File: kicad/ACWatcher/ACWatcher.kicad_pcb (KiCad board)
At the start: 2 copper layers, 7 parts, among them J1 Intake Temp Sensor, J2 Discharge Temp Sensor, J3 CT Clamp, U1 WeMos_D1_mini

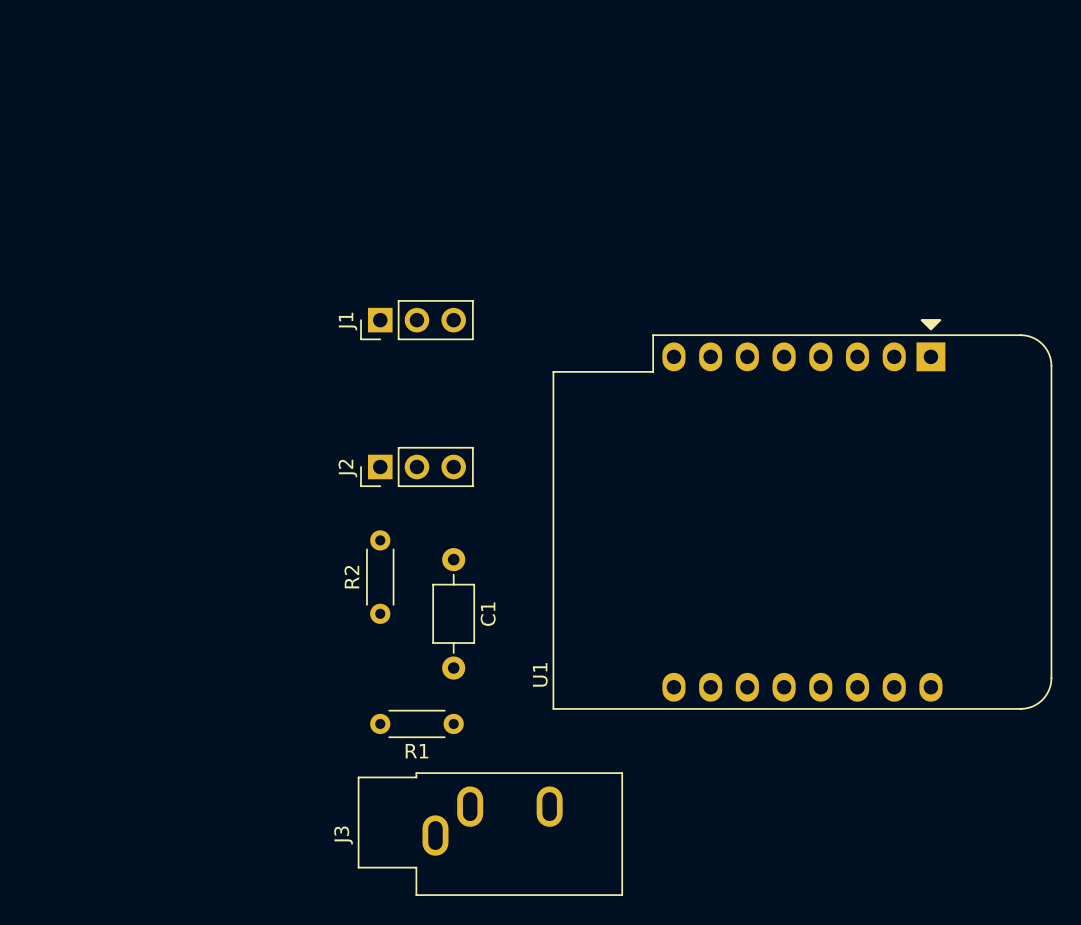
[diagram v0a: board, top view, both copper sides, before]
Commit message: Added 4.7k resistor for Dallas network
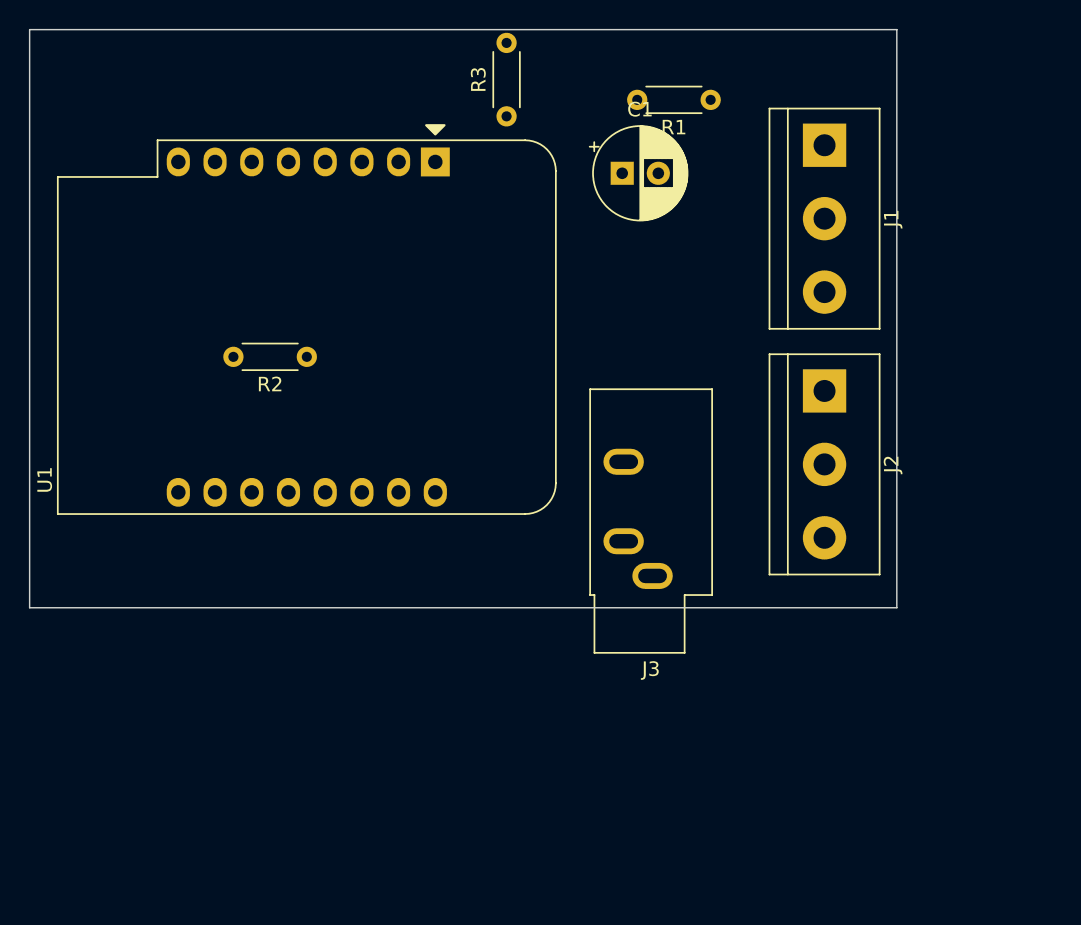
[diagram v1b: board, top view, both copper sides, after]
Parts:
- added R3: 4.7k, Resistor_THT:R_Axial_DIN0204_L3.6mm_D1.6mm_P5.08mm_Horizontal, F.Cu at (57.0, 24.0)
- C1: footprint Capacitor_THT:C_Axial_L3.8mm_D2.6mm_P7.50mm_Horizontal -> Capacitor_THT:CP_Radial_D6.3mm_P2.50mm
- J1, J2: footprint Connector_PinHeader_2.54mm:PinHeader_1x03_P2.54mm_Vertical -> TerminalBlock:TerminalBlock_bornier-3_P5.08mm
- moved R1 46.7 mm to (71.1, 22.9)
- moved U1 36.8 mm to (52.1, 27.2)
- moved J1 33.0 mm to (79.0, 26.0), turned to -90 degrees
- moved J2 31.2 mm to (79.0, 43.0), turned to -90 degrees
- moved C1 29.2 mm to (65.0, 27.9), turned to 0 degrees
- moved J3 23.4 mm to (67.1, 55.8), turned to 180 degrees
- moved R2 18.5 mm to (43.2, 40.6), turned to 180 degrees
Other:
- board outline added: 60 x 40 mm
